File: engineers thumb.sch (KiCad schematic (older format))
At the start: 53 parts, among them J1 INPUT, J2 9V, J3 GND, J4 Out, J5 GND, J6 LED+, Q1 Q_PMOS_GSD, Q2 BC327, SW1 TREBLE_BOOST, U1 TL072, U2 TL072, U3 LM13700

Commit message: Corrected footprints
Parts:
- C10: renamed from C7; footprint Capacitor_THT:C_Rect_L7.2mm_W3.0mm_P5.00mm_FKS2_FKP2_MKS2_MKP2 -> 2.Breadboard components:C_Box_P5.08mm
- C2: renamed from C1; footprint Capacitor_THT:C_Rect_L7.2mm_W3.0mm_P5.00mm_FKS2_FKP2_MKS2_MKP2 -> 2.Breadboard components:C_Box_P5.08mm
- C3: renamed from C9; footprint Capacitor_THT:C_Rect_L7.2mm_W3.0mm_P5.00mm_FKS2_FKP2_MKS2_MKP2 -> 2.Breadboard components:C_Box_P5.08mm
- C4: renamed from C10; footprint Capacitor_THT:C_Rect_L7.2mm_W3.0mm_P5.00mm_FKS2_FKP2_MKS2_MKP2 -> 2.Breadboard components:C_Box_P5.08mm
- C6: renamed from C11; footprint Capacitor_THT:C_Rect_L7.2mm_W3.0mm_P5.00mm_FKS2_FKP2_MKS2_MKP2 -> 2.Breadboard components:C_Box_P5.08mm
- D1: footprint Diode_THT:D_DO-34_SOD68_P7.62mm_Horizontal -> LED_THT:LED_D3.0mm
- D2: renamed from D3; footprint Diode_THT:D_DO-34_SOD68_P7.62mm_Horizontal -> 2.Breadboard components:D_Axial_Small_P5.08mm
- D3: renamed from D2; footprint Diode_THT:D_DO-34_SOD68_P7.62mm_Horizontal -> LED_THT:LED_D3.0mm
- D4, D5: footprint Diode_THT:D_DO-34_SOD68_P7.62mm_Horizontal -> 2.Breadboard components:D_Axial_Small_P10.16mm
- Q1: footprint Package_TO_SOT_SMD:SOT-23 -> Package_TO_SOT_SMD:SOT-23W_Handsoldering
- R1, R11, R12, R13, R14, R15, R16, R17, R19, R2, R20, R4, R6, R7, R9: footprint Resistor_THT:R_Axial_DIN0207_L6.3mm_D2.5mm_P7.62mm_Horizontal -> 2.Breadboard components:R_Axial_L6mm_D2mm_P10.16mm
- R10, R3: footprint Resistor_THT:R_Axial_DIN0207_L6.3mm_D2.5mm_P15.24mm_Horizontal -> 2.Breadboard components:R_Axial_L6mm_D2mm_P10.16mm
- R18: footprint Resistor_THT:R_Axial_DIN0207_L6.3mm_D2.5mm_P2.54mm_Vertical -> 2.Breadboard components:R_Axial_L6mm_D2mm_P10.16mm
- R5: footprint Resistor_THT:R_Axial_DIN0207_L6.3mm_D2.5mm_P10.16mm_Horizontal -> 2.Breadboard components:R_Axial_L6mm_D2mm_P10.16mm
- R8: footprint Resistor_THT:R_Axial_DIN0207_L6.3mm_D2.5mm_P5.08mm_Vertical -> 2.Breadboard components:R_Axial_L6mm_D2mm_P10.16mm
- U1, U2: footprint Package_DIP:DIP-8_W7.62mm_Socket -> 2.Breadboard components:DIP-8_Socket
- U3: footprint Package_DIP:DIP-16_W7.62mm_Socket -> 2.Breadboard components:DIP-16_Socket
- renumbered C2 to C1, C8 to C11, C3 to C5, C4 to C7, C5 to C8, C6 to C9, J5 to J2, J2 to J3, J3 to J4, J6 to J5, J4 to J6

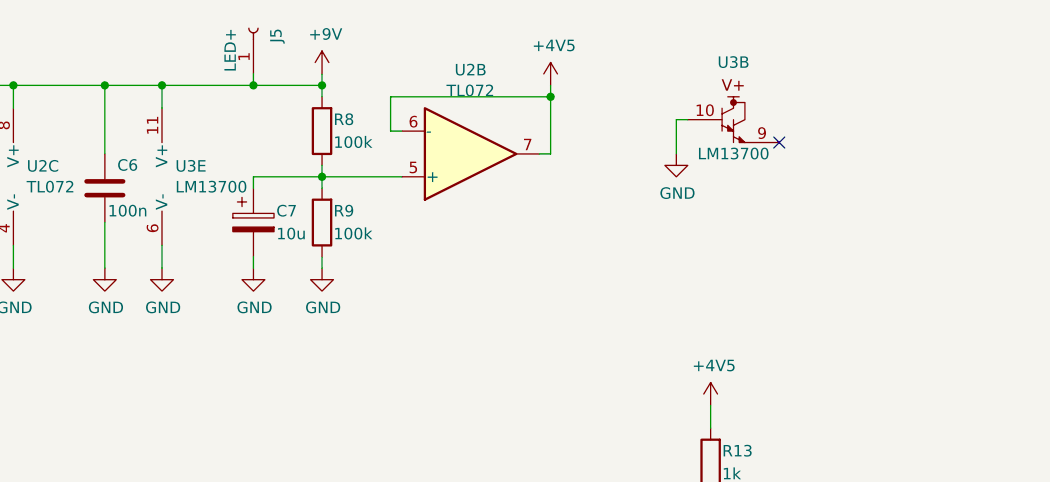
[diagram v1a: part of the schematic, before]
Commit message: updated layout
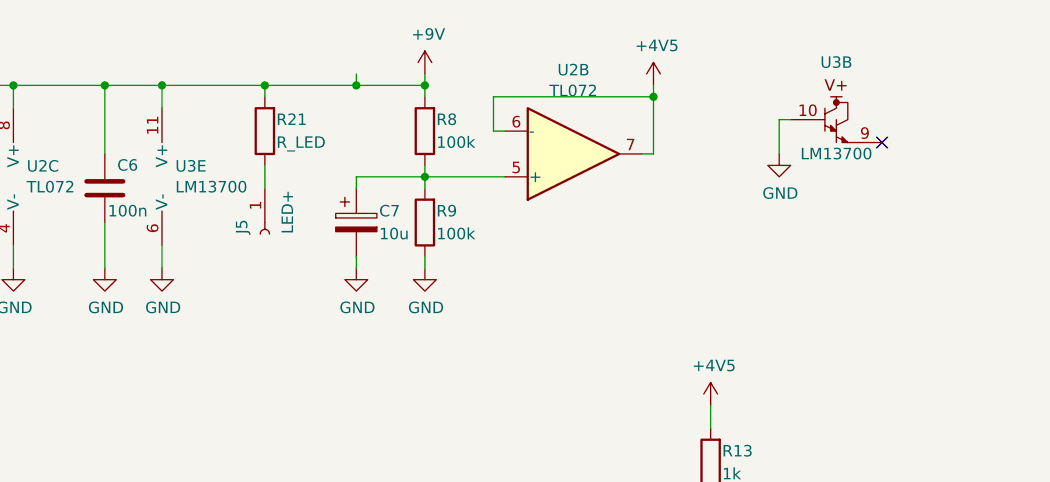
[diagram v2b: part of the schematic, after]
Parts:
- added R21: R_LED, 2.Breadboard components:R_Axial_Horizontal, symbol Device:R
- C1, C11, C7: footprint Capacitor_THT:CP_Radial_D6.3mm_P2.50mm -> 2.Breadboard components:CP_Vertical
- C5: footprint Capacitor_THT:C_Disc_D3.0mm_W1.6mm_P2.50mm -> 2.Breadboard components:C_Disc_P2.50mm
- C8, C9: footprint Capacitor_THT:CP_Radial_D5.0mm_P2.50mm -> 2.Breadboard components:CP_Vertical
- D1, D3: footprint LED_THT:LED_D3.0mm -> 2.Breadboard components:LED_D3.0mm_Vertical
- D2: footprint 2.Breadboard components:D_Axial_Small_P5.08mm -> 2.Breadboard components:D_Axial_Vertical
- D4, D5: footprint 2.Breadboard components:D_Axial_Small_P10.16mm -> 2.Breadboard components:D_Axial_Vertical
- R1, R10, R11, R12, R13, R14, R15, R16, R17, R19, R2, R20, R4, R5, R6, R7: footprint 2.Breadboard components:R_Axial_L6mm_D2mm_P10.16mm -> 2.Breadboard components:R_Axial_Horizontal
- R18, R3, R8, R9: footprint 2.Breadboard components:R_Axial_L6mm_D2mm_P10.16mm -> 2.Breadboard components:R_Axial_Vertical
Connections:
- net +9V: now also R21.2; no longer J5.1 (Pin_1)
- new net: J5.1 (Pin_1), R21.1
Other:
- moved on the sheet: C7, J5, R8, R9, U2B, U3B

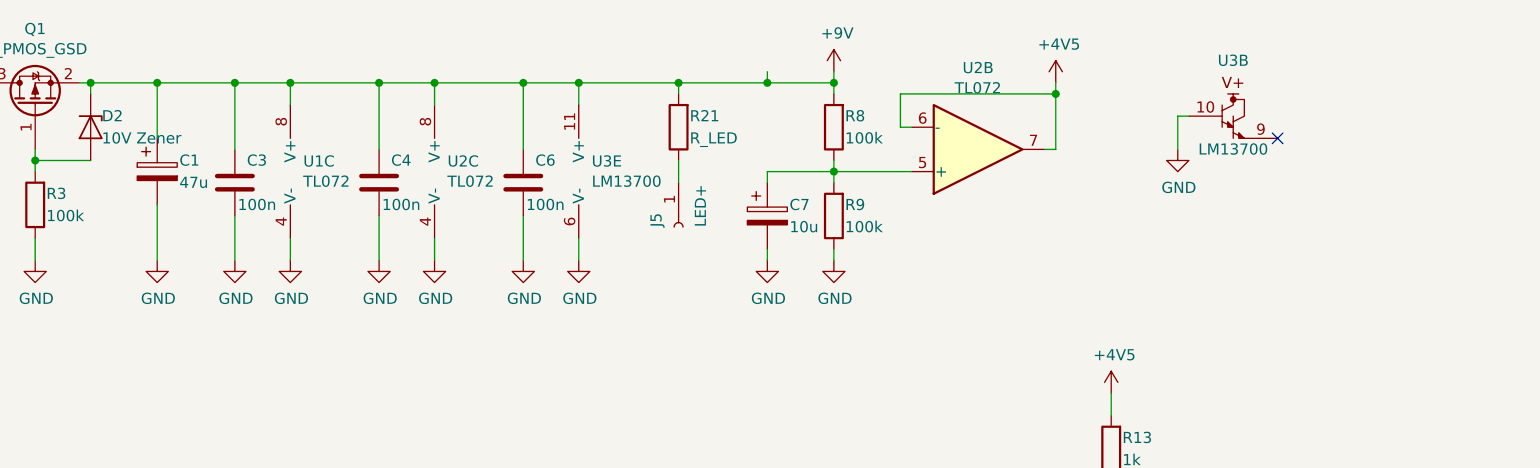
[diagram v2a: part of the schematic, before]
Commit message: added capacitor
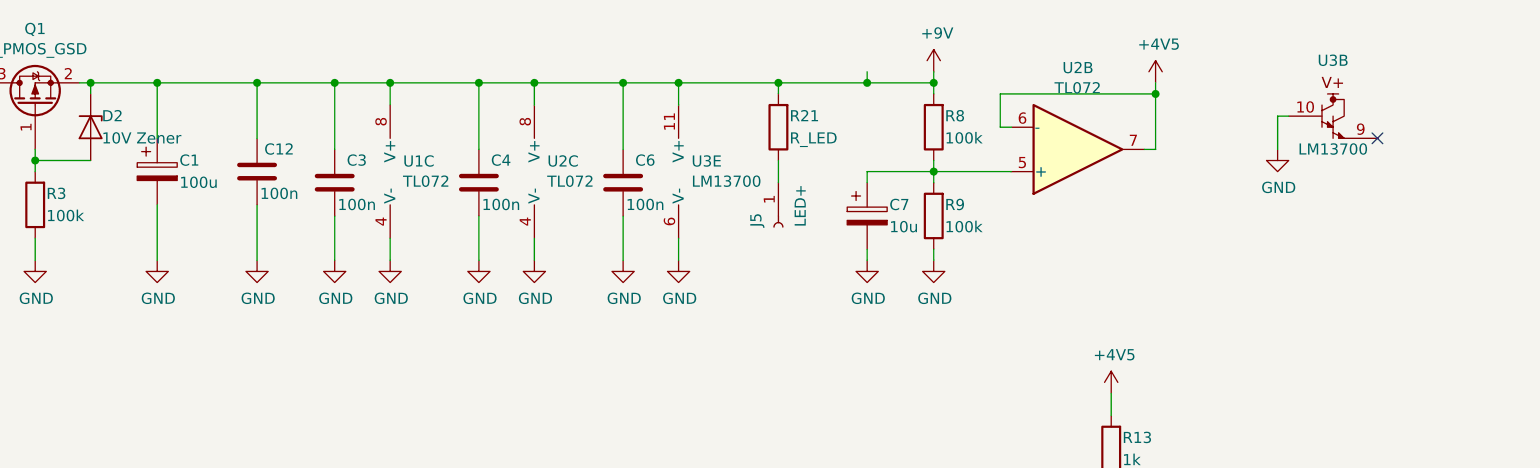
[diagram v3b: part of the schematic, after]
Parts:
- added C12: 100n, 2.Breadboard components:C_Box_P5.08mm, symbol Device:C
- C1: value 47u -> 100u
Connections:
- net +9V: now also C12.1
- net GND: now also C12.2
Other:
- moved on the sheet: C3, C4, C6, C7, J5, R21, R8, R9, U1C, U2B, U2C, U3B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

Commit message: Starting to do changes
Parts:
- removed J5: LED+, Connector_PinSocket_2.54mm:PinSocket_1x01_P2.54mm_Vertical, symbol Connector:Conn_01x01_Female
- removed R21: R_LED, 2.Breadboard components:R_Axial_Horizontal, symbol Device:R
- J1: value INPUT -> Conn_01x01; Field4 (none) -> Input
- J2, J4: value GND -> Conn_01x01; Field4 (none) -> GND
- J3: value 9V -> Conn_01x01; Field4 (none) -> 9V
- J6: value Out -> Conn_01x01; Field4 (none) -> Out
- RV1: value TH -> 1Meg_lin; Field4 (none) -> Thershold
- RV2: value RATIO -> 1Meg_log; Field4 (none) -> Ratio
- RV3: value REL -> 1Meg_lin; Field4 (none) -> Release
- RV4: value ATT -> 100k_log; Field4 (none) -> Attack
- RV5: value VOLUME -> 10k_log; Field4 (none) -> Volume
- SW1: value TREBLE_BOOST -> SPST; Field4 (none) -> Treble_boost
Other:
- moved on the sheet: C7, R8, R9, U2B, U3B

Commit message: Almost done
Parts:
- removed RV2: 1Meg_log, 1.Custom footprints:Alpha_16mm_potentiometer, symbol Device:R_POT
- removed RV3: 1Meg_lin, 1.Custom footprints:Alpha_16mm_potentiometer, symbol Device:R_POT
- removed RV4: 100k_log, 1.Custom footprints:Alpha_16mm_potentiometer, symbol Device:R_POT
- removed RV5: 10k_log, 1.Custom footprints:Alpha_16mm_potentiometer, symbol Device:R_POT
- removed SW1: SPST, 1.Custom footprints:PinSocket_2x01_P2.54mm_Vertical_Wide, symbol Switch:SW_SPST
- added J10, J11, J12, J5, J7, J8, J9: Conn_01x01, Connector_PinSocket_2.54mm:PinSocket_1x01_P2.54mm_Vertical, symbol Connector:Conn_01x01_Female
- D5: footprint 2.Breadboard components:D_Axial_Vertical -> 2.Breadboard components:D_Axial_Horizontal
- J2: Field4 GND -> VOL_1_&_TR_SW_2
- R1, R12, R2: footprint 2.Breadboard components:R_Axial_Horizontal -> 2.Breadboard components:R_Axial_Vertical
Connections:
- net +4V5: now also J2.1 (Pin_1)
- net GND: no longer J2.1 (Pin_1)
- net at C5.1, R11.1, R12.1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: now also R7.2
- net at U3.7: now also J11.1 (Pin_1)
- net at C5.2, R17.1, U1.1: now also J10.1 (Pin_1); no longer R7.2
- net at C10.1: now also J12.1 (Pin_1)
- net at R6.2: now also J7.1 (Pin_1)
- net at R5.2: now also J5.1 (Pin_1)
- net at C8.1, R10.1: now also J8.1 (Pin_1)
- net at R7.1: now also J9.1 (Pin_1)
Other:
- moved on the sheet: C11, D4, D5, J6, R19, R20, R5, R6, R7, U1B, U3D

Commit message: Finnished?
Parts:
- R1, R2, R8: footprint 2.Breadboard components:R_Axial_Vertical -> 2.Breadboard components:R_Axial_Horizontal
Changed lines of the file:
@@
 F 0 "R1" H 1200 5700 50  0000 C CNN
 F 1 "1M" H 1200 5600 50  0000 C CNN
-F 2 "2.Breadboard components:R_Axial_Vertical" V 1030 5700 50  0001 C CNN
+F 2 "2.Breadboard components:R_Axial_Horizontal" V 1030 5700 50  0001 C CNN
 F 3 "~" H 1100 5700 50  0001 C CNN
 	1    1100 5700
@@
 F 0 "R2" V 1450 5500 50  0000 R CNN
 F 1 "1k" V 1250 5500 50  0000 R CNN
-F 2 "2.Breadboard components:R_Axial_Vertical" V 1280 5450 50  0001 C CNN
+F 2 "2.Breadboard components:R_Axial_Horizontal" V 1280 5450 50  0001 C CNN
 F 3 "~" H 1350 5450 50  0001 C CNN
 	1    1350 5450
@@
 F 0 "R8" H 5050 1200 50  0000 R CNN
 F 1 "100k" H 5050 1300 50  0000 R CNN
-F 2 "2.Breadboard components:R_Axial_Vertical" V 5030 1250 50  0001 C CNN
+F 2 "2.Breadboard components:R_Axial_Horizontal" V 5030 1250 50  0001 C CNN
 F 3 "~" H 5100 1250 50  0001 C CNN
 	1    5100 1250

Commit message: Its never done
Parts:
- removed RV1: 1Meg_lin, 1.Custom footprints:Alpha_16mm_potentiometer, symbol Device:R_POT
- added J13, J14, J15: Conn_01x01, Connector_PinSocket_2.54mm:PinSocket_1x01_P2.54mm_Vertical, symbol Connector:Conn_01x01_Female
- R3, R9: footprint 2.Breadboard components:R_Axial_Vertical -> 2.Breadboard components:R_Axial_Horizontal
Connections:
- net at C2.1, U1.3 (+): now also J14.1 (Pin_1)
- net at R4.1: now also J13.1 (Pin_1)
- net at U1.5 (+): now also J15.1 (Pin_1)
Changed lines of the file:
@@
 	6000 4850 6350 4850
 Wire Wire Line
-	2250 3400 2250 3500
+	2250 3400 2250 3450
 Wire Wire Line
 	5900 4350 6000 4350
@@
 F 0 "R9" H 5050 1600 50  0000 R CNN
 F 1 "100k" H 5050 1700 50  0000 R CNN
-F 2 "2.Breadboard components:R_Axial_Vertical" V 5030 1650 50  0001 C CNN
+F 2 "2.Breadboard components:R_Axial_Horizontal" V 5030 1650 50  0001 C CNN
 F 3 "~" H 5100 1650 50  0001 C CNN
 	1    5100 1650
@@
 F 0 "R3" H 1350 1550 50  0000 R CNN
 F 1 "100k" H 1350 1650 50  0000 R CNN
-F 2 "2.Breadboard components:R_Axial_Vertical" V 1330 1600 50  0001 C CNN
+F 2 "2.Breadboard components:R_Axial_Horizontal" V 1330 1600 50  0001 C CNN
 F 3 "~" H 1400 1600 50  0001 C CNN
 	1    1400 1600
@@
 Connection ~ 2250 5450
 Wire Wire Line
-	2250 3800 2250 5450
+	2250 3800 2250 4000
 Wire Wire Line
 	7150 5400 7150 5350
@@
 	4550 3350 4550 3550
 $Comp
-L Device:R_POT RV1
+L Device:R_POT #RV1
 U 1 1 5E70AF1F
 P 2250 3650
-F 0 "RV1" H 2200 3600 50  0000 R CNN
+F 0 "#RV1" H 2200 3600 50  0000 R CNN
 F 1 "1Meg_lin" H 2200 3800 50  0000 R CNN
 F 2 "1.Custom footprints:Alpha_16mm_potentiometer" H 2250 3650 50  0001 C CNN
@@
 Connection ~ 3700 3050
 Wire Wire Line
-	2500 3650 2400 3650
+	2500 3650 2450 3650
 Wire Wire Line
 	3600 3550 3650 3550
@@
 Wire Wire Line
 	5450 4350 5500 4350
+$Comp
+L Connector:Conn_01x01_Female J13
+U 1 1 5EAE4D74
+P 1950 3450
+F 0 "J13" H 1950 3350 50  0000 L CNN
+F 1 "Conn_01x01" H 1950 3450 50  0000 L CNN
+F 2 "Connector_PinSocket_2.54mm:PinSocket_1x01_P2.54mm_Vertical" H 1950 3450 50  0001 C CNN
+F 3 "~" H 1950 3450 50  0001 C CNN
+F 4 "TH_1" H 1950 3550 50  0000 L CNN "Field4"
+	1    1950 3450
+	-1   0    0    1
+$EndComp
+$Comp
+L Connector:Conn_01x01_Female J14
+U 1 1 5EAE8B09
+P 1950 4000
+F 0 "J14" H 1950 3900 50  0000 L CNN
+F 1 "Conn_01x01" H 1950 4000 50  0000 L CNN
+F 2 "Connector_PinSocket_2.54mm:PinSocket_1x01_P2.54mm_Vertical" H 1950 4000 50  0001 C CNN
+F 3 "~" H 1950 4000 50  0001 C CNN
+F 4 "TH_3" H 1950 4100 50  0000 L CNN "Field4"
+	1    1950 4000
+	-1   0    0    1
+$EndComp
+$Comp
+L Connector:Conn_01x01_Female J15
+U 1 1 5EAE96BE
+P 2450 3900
+F 0 "J15" H 2450 3800 50  0000 L CNN
+F 1 "Conn_01x01" H 2450 3900 50  0000 L CNN
+F 2 "Connector_PinSocket_2.54mm:PinSocket_1x01_P2.54mm_Vertical" H 2450 3900 50  0001 C CNN
+F 3 "~" H 2450 3900 50  0001 C CNN
+F 4 "TH_1" H 2450 4000 50  0000 L CNN "Field4"
+	1    2450 3900
+	0    1    1    0
+$EndComp
+Wire Wire Line
+	2450 3700 2450 3650
+Connection ~ 2450 3650
+Wire Wire Line
+	2450 3650 2400 3650
+Wire Wire Line
+	2150 3450 2250 3450
+Connection ~ 2250 3450
+Wire Wire Line
+	2250 3450 2250 3500
+Wire Wire Line
+	2150 4000 2250 4000
+Connection ~ 2250 4000
+Wire Wire Line
+	2250 4000 2250 5450
 $EndSCHEMATC

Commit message: its never done
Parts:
- removed C12: 100n, 2.Breadboard components:C_Box_P5.08mm, symbol Device:C
- added D6, D7: 1N4007, Diode_THT:D_DO-35_SOD27_P7.62mm_Horizontal, symbol Device:D
- C1, C11, C7, C8, C9: footprint 2.Breadboard components:CP_Vertical -> Capacitor_THT:CP_Radial_D6.3mm_P2.50mm
- D1, D3: footprint 2.Breadboard components:LED_D3.0mm_Vertical -> LED_THT:LED_D3.0mm
- D2, D4: footprint 2.Breadboard components:D_Axial_Vertical -> Diode_THT:D_DO-35_SOD27_P7.62mm_Horizontal
- D5: footprint 2.Breadboard components:D_Axial_Horizontal -> Diode_THT:D_DO-35_SOD27_P7.62mm_Horizontal
- Q1: value Q_PMOS_GSD -> DMP3099L
- R1, R10, R11, R13, R14, R15, R16, R17, R19, R2, R20, R3, R4, R5, R6, R7, R8, R9: footprint 2.Breadboard components:R_Axial_Horizontal -> Resistor_THT:R_Axial_DIN0204_L3.6mm_D1.6mm_P7.62mm_Horizontal
- R12, R18: footprint 2.Breadboard components:R_Axial_Vertical -> Resistor_THT:R_Axial_DIN0204_L3.6mm_D1.6mm_P7.62mm_Horizontal
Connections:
- net +9V: now also D6.1 (K), D7.1 (K)
- net GND: now also D7.2 (A)
- net at J3.1 (Pin_1), Q1.3 (D): now also D6.2 (A)
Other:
- moved on the sheet: C1
